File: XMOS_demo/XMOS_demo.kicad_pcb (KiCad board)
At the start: 4 copper layers, 100 x 100 mm, 210 parts, among them J1 XSYS2 DEBUG CONNECTOR, J10 Conn_PMOD_02x06, J11 Conn_PMOD_02x06, J2 Screw_Terminal, J3 Conn_01x02_Pin, J4 USB_C_Receptacle_USB2.0_16P, J5 Conn_01x06_Socket, J6 Conn_01x06_Socket, J7 AudioJack3_SwitchT, J8 AudioJack2_SwitchT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

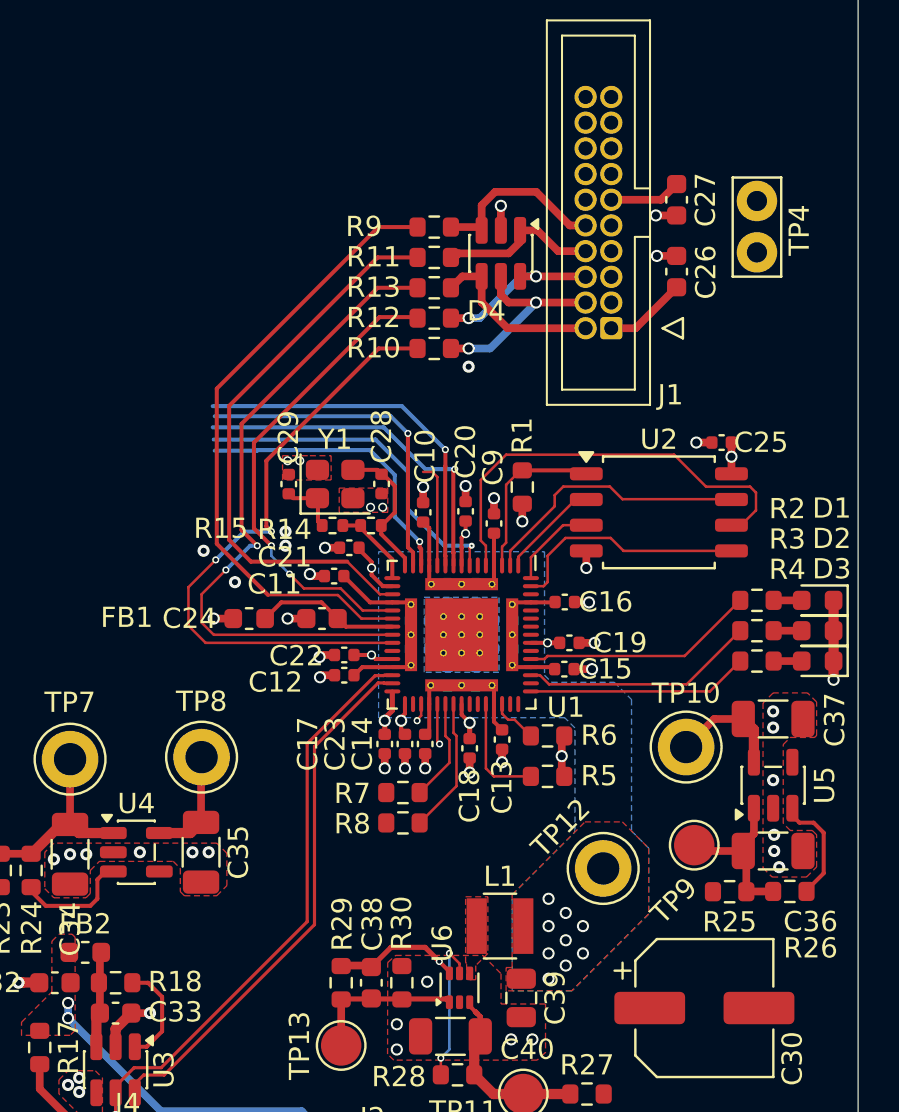
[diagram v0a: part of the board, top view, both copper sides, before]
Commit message: Changed flash to correct part
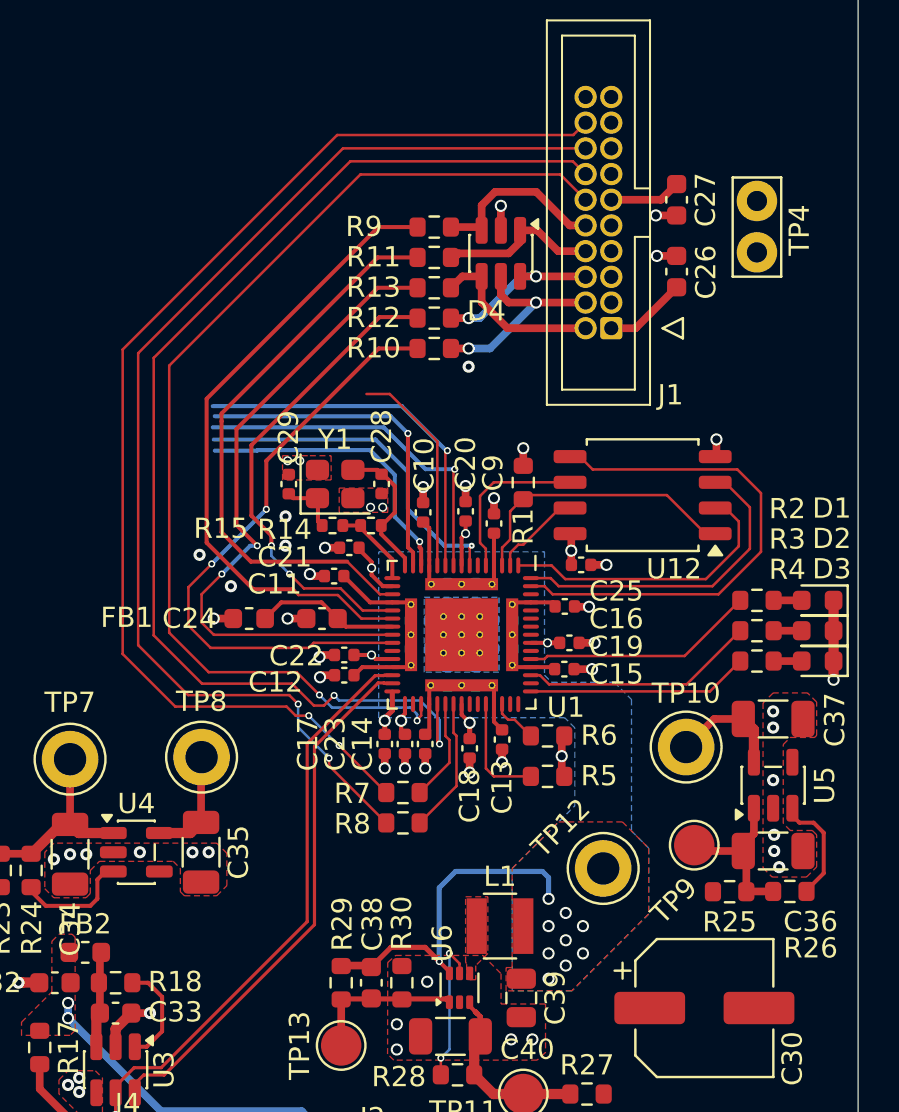
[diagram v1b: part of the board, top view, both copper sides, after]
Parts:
- removed U2: W25Q32JVSS, Package_SO:SOIC-8_5.3x5.3mm_P1.27mm
- added U12: AT25FF161A, Package_SO:SOIC-8_5.3x5.3mm_P1.27mm, F.Cu at (181.3, 113.0)
- moved C25 9.21 mm to (178.3, 116.4), turned to 180 degrees
- moved R1 0.23 mm to (175.4, 112.4), turned to 90 degrees
- moved C16 0.22 mm to (177.5, 118.5)
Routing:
- net /MCU/XL0_OUT1: track 0.00 -> 58.4 mm, vias 0 -> 2
- net /MCU/XL0_OUT0: track 0.00 -> 57.5 mm, vias 0 -> 2
- net /MCU/XL0_IN0: track 2.02 -> 58.8 mm, vias 1 -> 2
- net /MCU/XL0_IN1: track 0.86 -> 53.3 mm, vias 1 -> 2
- net /MCU/QSPI_D0: track 11.9 -> 25.5 mm
- net /MCU/QSPI_CLK: track 21.6 -> 8.98 mm
- net /MCU/QSPI_D2: track 4.42 -> 16.0 mm
- net P0V9: track 29.6 -> 40.2 mm
- net /MCU/QSPI_D1: track 4.96 -> 14.5 mm
- net /MCU/QSPI_D3: track 13.6 -> 4.50 mm
- net /MCU/QSPI_~{CS}: track 8.40 -> 14.1 mm
- net /MCU/CODEC_~{RST}: track 5.18 -> 10.6 mm
- net /MCU/TCK: track 30.9 -> 30.2 mm
- net /MCU/RST_N: track 31.1 -> 31.8 mm

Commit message: routing work
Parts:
- moved C55 15.1 mm to (126.6, 66.0)
- moved C43 15.1 mm to (129.6, 66.0)
- moved R36 14.9 mm to (120.8, 70.2)
- moved R37 14.9 mm to (120.8, 68.7)
- moved C42 14.6 mm to (125.0, 72.5)
- moved C44 14.6 mm to (123.5, 67.5)
- moved C56 14.6 mm to (128.0, 72.5)
- moved C58 14.6 mm to (130.0, 70.0)
- moved R31 14.6 mm to (125.0, 74.5)
- moved R38 14.6 mm to (128.5, 63.8)
- moved R39 14.6 mm to (121.6, 72.7)
- moved U7 14.6 mm to (126.8, 69.4)
- moved R33 11.6 mm to (132.9, 67.5)
- moved R35 11.6 mm to (132.9, 66.0)
- moved RN2 9.85 mm to (110.9, 72.0)
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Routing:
- net /MCU/I2S_SCLK_OUT: track 14.4 -> 82.9 mm
- net /MCU/I2S_ADC_IN: track 17.0 -> 84.2 mm
- net /MCU/I2S_DAC_OUT: track 17.6 -> 82.9 mm
- net /MCU/MCLK_OUT: track 16.5 -> 79.1 mm
- net /MCU/I2S_LRCK_OUT: track 18.2 -> 78.4 mm
- net P1V8: track 16.0 -> 66.8 mm, vias 3 -> 5
- net /Codec/SDA: track 8.54 -> 56.7 mm, vias 0 -> 2
- net /Codec/I2S_SCLK_IN: track 0.00 -> 48.0 mm, vias 0 -> 1
- net /Codec/SCL: track 12.0 -> 57.1 mm, vias 0 -> 2
- net /Codec/I2S_ADC_OUT: track 0.00 -> 38.6 mm
- net /Codec/MCLK_IN: track 0.00 -> 35.3 mm
- net /I2S_Confing/I2S_SCLK_PMOD2: track 0.00 -> 34.1 mm
- net /Codec/I2S_DAC_IN: track 0.00 -> 31.6 mm
- net /I2S_Confing/I2S_ADC_PMOD2: track 0.00 -> 28.9 mm
- net P3V3: track 28.5 -> 56.0 mm, vias 7 -> 14
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- added copper zone on B.Cu, net P3V3

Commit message: pdf documentation
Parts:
- moved R23 41.8 mm to (189.8, 134.3), turned to 0 degrees
- moved R24 40.3 mm to (189.8, 132.8), turned to 0 degrees
- moved R26 39.5 mm to (149.1, 132.1), turned to -90 degrees
- moved R25 38.0 mm to (147.6, 132.1), turned to -90 degrees
- moved C34 37.5 mm to (189.0, 130.9), turned to 0 degrees
- moved C36 36.7 mm to (151.2, 131.3), turned to -90 degrees
- moved TP7 36.6 mm to (184.5, 130.9), turned to -90 degrees
- moved TP9 35.5 mm to (148.4, 129.0), turned to -90 degrees
- moved U4 34.3 mm to (188.9, 127.6), turned to 90 degrees
- moved U5 33.6 mm to (154.4, 131.3), turned to 0 degrees
- moved C35 31.6 mm to (188.9, 124.4), turned to 0 degrees
- moved C37 31.0 mm to (157.7, 131.3), turned to -90 degrees
- moved TP8 23.6 mm to (184.5, 125.3), turned to 90 degrees
- moved TP10 22.8 mm to (161.1, 129.8), turned to 0 degrees
- moved C31 3.51 mm to (143.2, 136.0)
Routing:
- net P1V8: track 66.8 -> 44.7 mm, vias 5 -> 3
- net P3V3: track 56.0 -> 38.1 mm, vias 14 -> 11
- net Net-(U5-IN): track 8.02 -> 2.08 mm
- added copper zone on F.Cu, net P3V3
